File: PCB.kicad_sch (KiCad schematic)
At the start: 10 parts

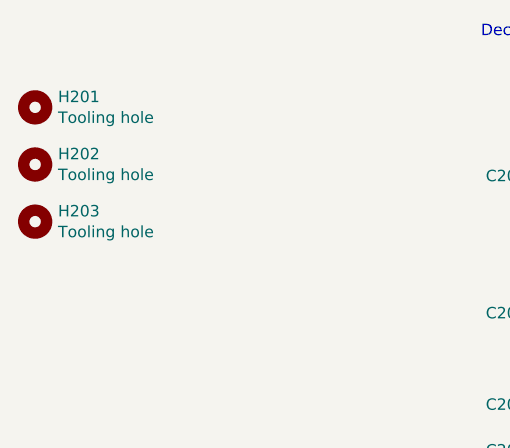
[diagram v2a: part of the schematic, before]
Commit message: Remove tooling holes
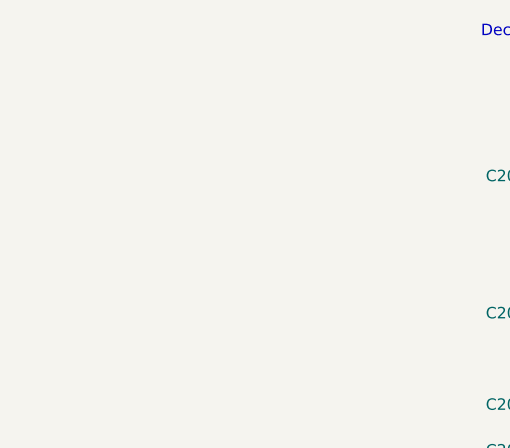
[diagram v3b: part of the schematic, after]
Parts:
- removed H201, H202, H203: Tooling hole, SH-ESP32-tank-hat:JlcpcbToolingHole, symbol Mechanical:MountingHole
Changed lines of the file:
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@@
     (pin "1")
   )
-  (symbol (lib_id "Mechanical:MountingHole") (at 38.1 41.91 0) (unit 1)
-    (in_bom yes) (on_board yes)
-    (property "Reference" "H201" (id 0) (at 40.64 40.7416 0)
-      (effects (font (size 1.27 1.27)) (justify left))
-    )
-    (property "Value" "Tooling hole" (id 1) (at 40.64 43.053 0)
-      (effects (font (size 1.27 1.27)) (justify left))
-    )
-    (property "Footprint" "SH-ESP32-tank-hat:JlcpcbToolingHole" (id 2) (at 38.1 41.91 0)
-      (effects (font (size 1.27 1.27)) hide)
-    )
-    (property "Datasheet" "~" (id 3) (at 38.1 41.91 0)
-      (effects (font (size 1.27 1.27)) hide)
-    )
-  )
-  (symbol (lib_id "Mechanical:MountingHole") (at 38.1 48.26 0) (unit 1)
-    (in_bom yes) (on_board yes)
-    (property "Reference" "H202" (id 0) (at 40.64 47.0916 0)
-      (effects (font (size 1.27 1.27)) (justify left))
-    )
-    (property "Value" "Tooling hole" (id 1) (at 40.64 49.403 0)
-      (effects (font (size 1.27 1.27)) (justify left))
-    )
-    (property "Footprint" "SH-ESP32-tank-hat:JlcpcbToolingHole" (id 2) (at 38.1 48.26 0)
-      (effects (font (size 1.27 1.27)) hide)
-    )
-    (property "Datasheet" "~" (id 3) (at 38.1 48.26 0)
-      (effects (font (size 1.27 1.27)) hide)
-    )
-  )
-  (symbol (lib_id "Mechanical:MountingHole") (at 38.1 54.61 0) (unit 1)
-    (in_bom yes) (on_board yes)
-    (property "Reference" "H203" (id 0) (at 40.64 53.4416 0)
-      (effects (font (size 1.27 1.27)) (justify left))
-    )
-    (property "Value" "Tooling hole" (id 1) (at 40.64 55.753 0)
-      (effects (font (size 1.27 1.27)) (justify left))
-    )
-    (property "Footprint" "SH-ESP32-tank-hat:JlcpcbToolingHole" (id 2) (at 38.1 54.61 0)
-      (effects (font (size 1.27 1.27)) hide)
-    )
-    (property "Datasheet" "~" (id 3) (at 38.1 54.61 0)
-      (effects (font (size 1.27 1.27)) hide)
-    )
-  )
 )

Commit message: Add PCB graphics as symbols
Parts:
- added G501: CC-BY, SH-ESP32-tank-hat:cc-by_5mm, symbol SH-ESP32-engine-hat:Image
- added G502: CE-logo, Symbol:CE-Logo_11.2x8mm_SilkScreen, symbol SH-ESP32-engine-hat:Image
- added G503: WEEE-logo, Symbol:WEEE-Logo_5.6x8mm_SilkScreen, symbol SH-ESP32-engine-hat:Image
- added G504: OSHW-logo, Symbol:OSHW-Logo2_9.8x8mm_SilkScreen, symbol SH-ESP32-engine-hat:Image
- added G505: HL-Logo, SH-ESP32-tank-hat:Hat_Labs_20mm, symbol SH-ESP32-engine-hat:Image
- renumbered C201 to C501, C202 to C502, C203 to C503, C204 to C504, C205 to C505, C206 to C506, C207 to C507
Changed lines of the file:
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@@
   (symbol (lib_id "Device:C") (at 95.25 52.07 90) (mirror x) (unit 1)
     (in_bom yes) (on_board yes)
-    (property "Reference" "C201" (id 0) (at 92.71 49.53 90)
+    (property "Reference" "C501" (id 0) (at 92.71 49.53 90)
       (effects (font (size 1.27 1.27)) (justify left))
     )
@@
   (symbol (lib_id "Device:C") (at 95.25 67.31 90) (mirror x) (unit 1)
     (in_bom yes) (on_board yes)
-    (property "Reference" "C202" (id 0) (at 92.71 64.77 90)
+    (property "Reference" "C502" (id 0) (at 92.71 64.77 90)
       (effects (font (size 1.27 1.27)) (justify left))
     )
@@
   (symbol (lib_id "Device:C") (at 95.25 77.47 90) (mirror x) (unit 1)
     (in_bom yes) (on_board yes)
-    (property "Reference" "C203" (id 0) (at 92.71 74.93 90)
+    (property "Reference" "C503" (id 0) (at 92.71 74.93 90)
       (effects (font (size 1.27 1.27)) (justify left))
     )
@@
   (symbol (lib_id "Device:C") (at 95.25 82.55 90) (mirror x) (unit 1)
     (in_bom yes) (on_board yes)
-    (property "Reference" "C204" (id 0) (at 92.71 80.01 90)
+    (property "Reference" "C504" (id 0) (at 92.71 80.01 90)
       (effects (font (size 1.27 1.27)) (justify left))
     )
@@
   (symbol (lib_id "Device:C") (at 95.25 87.63 90) (mirror x) (unit 1)
     (in_bom yes) (on_board yes)
-    (property "Reference" "C205" (id 0) (at 92.71 85.09 90)
+    (property "Reference" "C505" (id 0) (at 92.71 85.09 90)
       (effects (font (size 1.27 1.27)) (justify left))
     )
@@
   (symbol (lib_id "Device:C") (at 95.25 92.71 90) (mirror x) (unit 1)
     (in_bom yes) (on_board yes)
-    (property "Reference" "C206" (id 0) (at 92.71 90.17 90)
+    (property "Reference" "C506" (id 0) (at 92.71 90.17 90)
       (effects (font (size 1.27 1.27)) (justify left))
     )
@@
   (symbol (lib_id "Device:C") (at 95.25 97.79 90) (mirror x) (unit 1)
     (in_bom yes) (on_board yes)
-    (property "Reference" "C207" (id 0) (at 92.71 95.25 90)
+    (property "Reference" "C507" (id 0) (at 92.71 95.25 90)
       (effects (font (size 1.27 1.27)) (justify left))
     )
@@
   (symbol (lib_id "power:+3.3V") (at 99.06 41.91 0) (unit 1)
     (in_bom yes) (on_board yes)
-    (property "Reference" "#PWR0202" (id 0) (at 99.06 45.72 0)
+    (property "Reference" "#PWR0502" (id 0) (at 99.06 45.72 0)
       (effects (font (size 1.27 1.27)) hide)
     )
@@
   (symbol (lib_id "power:GND") (at 91.44 106.68 0) (unit 1)
     (in_bom yes) (on_board yes)
-    (property "Reference" "#PWR0201" (id 0) (at 91.44 113.03 0)
+    (property "Reference" "#PWR0501" (id 0) (at 91.44 113.03 0)
       (effects (font (size 1.27 1.27)) hide)
     )
@@
   (symbol (lib_id "power:PWR_FLAG") (at 91.44 105.41 90) (unit 1)
     (in_bom yes) (on_board yes)
-    (property "Reference" "#FLG0201" (id 0) (at 89.535 105.41 0)
+    (property "Reference" "#FLG0501" (id 0) (at 89.535 105.41 0)
       (effects (font (size 1.27 1.27)) hide)
     )
@@
     (pin "1")
   )
+  (symbol (lib_id "SH-ESP32-engine-hat:Image") (at 140.97 54.61 0) (unit 1)
+    (in_bom no) (on_board yes) (fields_autoplaced)
+    (property "Reference" "G502" (id 0) (at 144.78 53.3399 0)
+      (effects (font (size 1.27 1.27)) (justify left))
+    )
+    (property "Value" "CE-logo" (id 1) (at 144.78 55.8799 0)
+      (effects (font (size 1.27 1.27)) (justify left))
+    )
+    (property "Footprint" "Symbol:CE-Logo_11.2x8mm_SilkScreen" (id 2) (at 140.97 54.61 0)
+      (effects (font (size 1.27 1.27)) hide)
+    )
+    (property "Datasheet" "" (id 3) (at 140.97 54.61 0)
+      (effects (font (size 1.27 1.27)) hide)
+    )
+  )
+  (symbol (lib_id "SH-ESP32-engine-hat:Image") (at 140.97 72.39 0) (unit 1)
+    (in_bom no) (on_board yes) (fields_autoplaced)
+    (property "Reference" "G504" (id 0) (at 144.78 71.1199 0)
+      (effects (font (size 1.27 1.27)) (justify left))
+    )
+    (property "Value" "OSHW-logo" (id 1) (at 144.78 73.6599 0)
+      (effects (font (size 1.27 1.27)) (justify left))
+    )
+    (property "Footprint" "Symbol:OSHW-Logo2_9.8x8mm_SilkScreen" (id 2) (at 140.97 72.39 0)
+      (effects (font (size 1.27 1.27)) hide)
+    )
+    (property "Datasheet" "" (id 3) (at 140.97 72.39 0)
+      (effects (font (size 1.27 1.27)) hide)
+    )
+  )
+  (symbol (lib_id "SH-ESP32-engine-hat:Image") (at 140.97 45.72 0) (unit 1)
+    (in_bom no) (on_board yes) (fields_autoplaced)
+    (property "Reference" "G501" (id 0) (at 144.78 44.4499 0)
+      (effects (font (size 1.27 1.27)) (justify left))
+    )
+    (property "Value" "CC-BY" (id 1) (at 144.78 46.9899 0)
+      (effects (font (size 1.27 1.27)) (justify left))
+    )
+    (property "Footprint" "SH-ESP32-tank-hat:cc-by_5mm" (id 2) (at 140.97 45.72 0)
+      (effects (font (size 1.27 1.27)) hide)
+    )
+    (property "Datasheet" "" (id 3) (at 140.97 45.72 0)
+      (effects (font (size 1.27 1.27)) hide)
+    )
+  )
+  (symbol (lib_id "SH-ESP32-engine-hat:Image") (at 140.97 81.28 0) (unit 1)
+    (in_bom no) (on_board yes) (fields_autoplaced)
+    (property "Reference" "G505" (id 0) (at 144.78 80.0099 0)
+      (effects (font (size 1.27 1.27)) (justify left))
+    )
+    (property "Value" "HL-Logo" (id 1) (at 144.78 82.5499 0)
+      (effects (font (size 1.27 1.27)) (justify left))
+    )
+    (property "Footprint" "SH-ESP32-tank-hat:Hat_Labs_20mm" (id 2) (at 140.97 81.28 0)
+      (effects (font (size 1.27 1.27)) hide)
+    )
+    (property "Datasheet" "" (id 3) (at 140.97 81.28 0)
+      (effects (font (size 1.27 1.27)) hide)
+    )
+  )
+  (symbol (lib_id "SH-ESP32-engine-hat:Image") (at 140.97 63.5 0) (unit 1)
+    (in_bom no) (on_board yes) (fields_autoplaced)
+    (property "Reference" "G503" (id 0) (at 144.78 62.2299 0)
+      (effects (font (size 1.27 1.27)) (justify left))
+    )
+    (property "Value" "WEEE-logo" (id 1) (at 144.78 64.7699 0)
+      (effects (font (size 1.27 1.27)) (justify left))
+    )
+    (property "Footprint" "Symbol:WEEE-Logo_5.6x8mm_SilkScreen" (id 2) (at 140.97 63.5 0)
+      (effects (font (size 1.27 1.27)) hide)
+    )
+    (property "Datasheet" "" (id 3) (at 140.97 63.5 0)
+      (effects (font (size 1.27 1.27)) hide)
+    )
+  )
 )
